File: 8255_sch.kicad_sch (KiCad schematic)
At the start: 3 parts, among them U2 8255, U5 8255, U6 8255

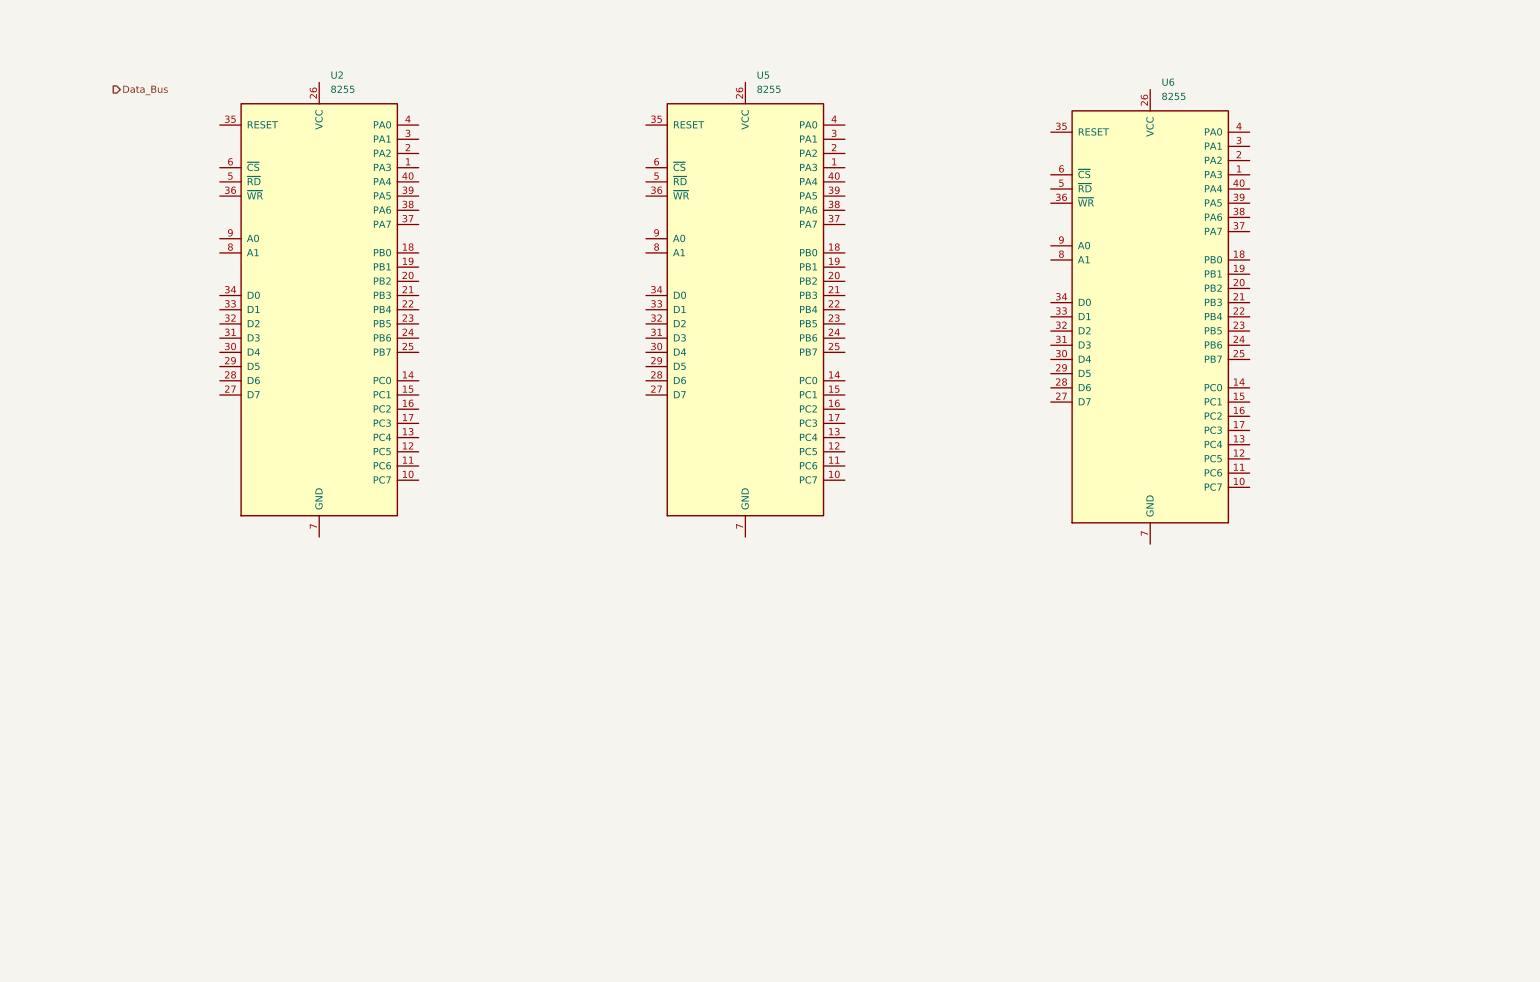
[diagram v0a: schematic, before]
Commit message: Wired up Decoding of 8255s, 8254, and 8279
Also fixed up the decoding for the 16550 and the 8259 as well as labeled all wires into/from the bus.
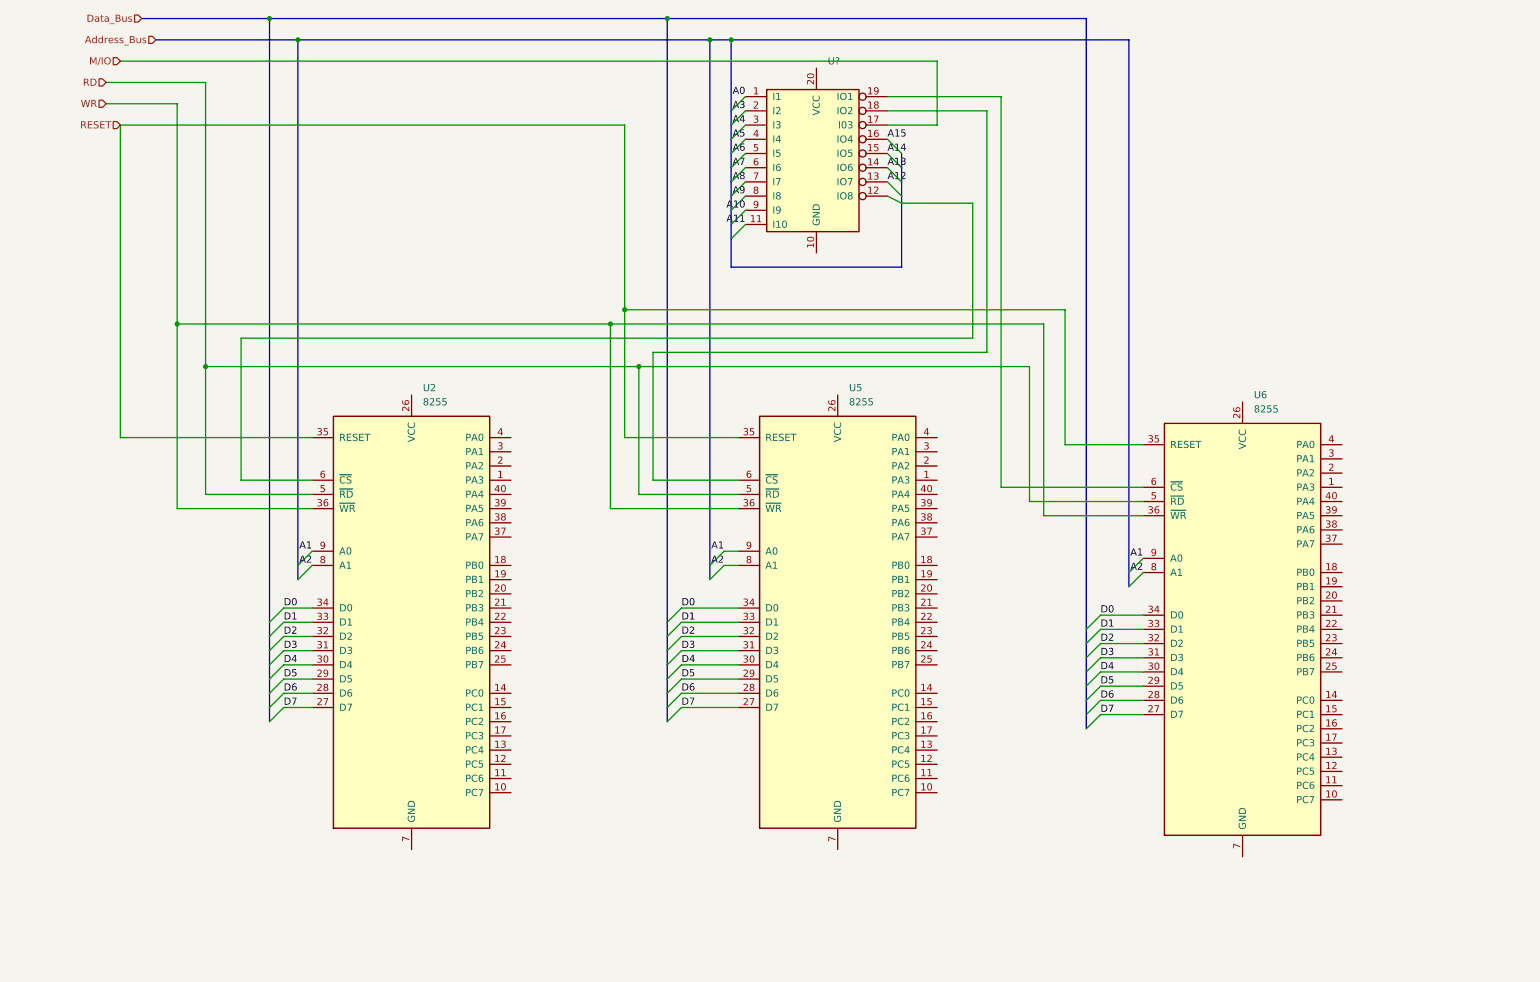
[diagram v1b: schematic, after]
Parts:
- added U?: (no value), symbol Logic_Programmable:PAL16L8
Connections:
- net D7: now reaches U2.27 (D7)
- net D7: now also U5.27 (D7), U6.27 (D7)
- net D6: now reaches U2.28 (D6)
- net D6: now also U5.28 (D6), U6.28 (D6)
- net D5: now reaches U2.29 (D5)
- net D5: now also U5.29 (D5), U6.29 (D5)
- net D4: now reaches U2.30 (D4)
- net D4: now also U5.30 (D4), U6.30 (D4)
- net D3: now reaches U2.31 (D3)
- net D3: now also U5.31 (D3), U6.31 (D3)
- net D2: now reaches U2.32 (D2)
- net D2: now also U5.32 (D2), U6.32 (D2)
- net D1: now reaches U2.33 (D1)
- net D1: now also U5.33 (D1), U6.33 (D1)
- net D0: now reaches U2.34 (D0)
- net D0: now also U5.34 (D0), U6.34 (D0)
- net RESET: now reaches U2.35 (RESET)
- net RESET: now also U5.35 (RESET), U6.35 (RESET)
- net WR: now reaches U2.36 (~{WR})
- net WR: now also U5.36 (~{WR}), U6.36 (~{WR})
- net RD: now reaches U2.5 (~{RD})
- net RD: now also U5.5 (~{RD}), U6.5 (~{RD})
- net at U2.6 (~{CS}): now also U?.12 (IO8)
- net A2: now reaches U2.8 (A1)
- net A2: now also U5.8 (A1), U6.8 (A1)
- net A1: now reaches U2.9 (A0)
- net A1: now also U5.9 (A0), U6.9 (A0)
- net at U6.6 (~{CS}): now also U?.19 (IO1)
- net at U5.6 (~{CS}): now also U?.18 (IO2)
- new net A0: U?.1 (I1)
- new net A10: U?.9 (I9)
- new net A11: U?.11 (I10)
- new net A12: U?.13 (IO7)
- new net A13: U?.14 (IO6)
- new net A14: U?.15 (IO5)
- new net A15: U?.16 (IO4)
- new net A3: U?.2 (I2)
- new net A4: U?.3 (I3)
- new net A5: U?.4 (I4)
- new net A6: U?.5 (I5)
- new net A7: U?.6 (I6)
- new net A8: U?.7 (I7)
- new net A9: U?.8 (I8)
- new net M/IO: U?.17 (I03)
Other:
- moved on the sheet: U2, U5, U6

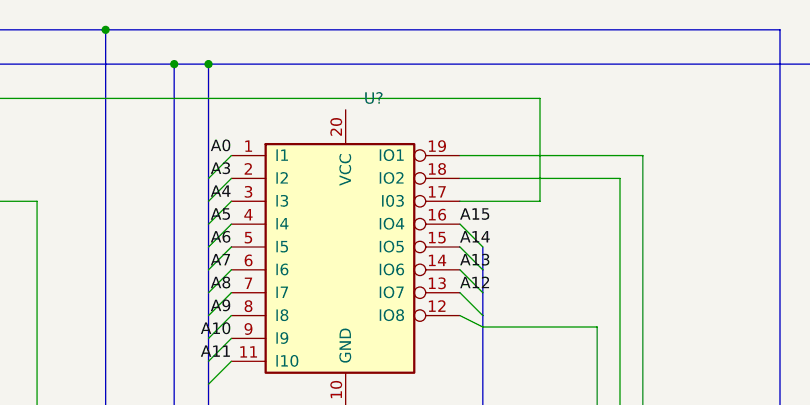
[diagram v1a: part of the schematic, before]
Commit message: Wired the max235 and DSUB9
We will double check the wiring tomorrow. Also added the data bus
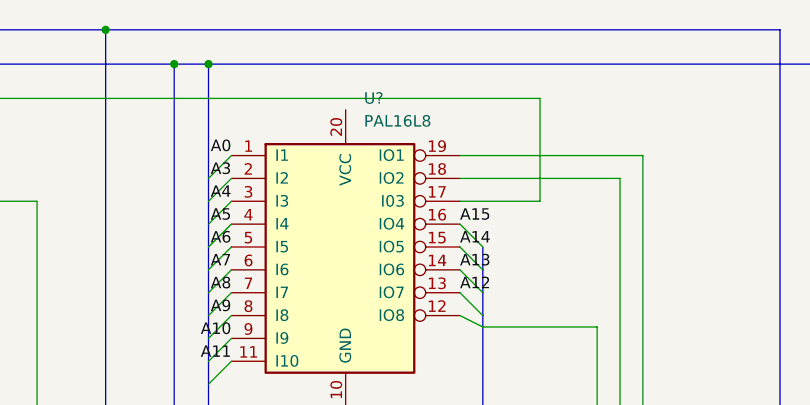
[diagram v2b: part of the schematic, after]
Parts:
- U?: value (none) -> PAL16L8
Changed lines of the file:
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@@
       (effects (font (size 1.27 1.27)) (justify left))
     )
-    (property "Value" "" (id 1) (at 149.3394 26.67 0)
+    (property "Value" "PAL16L8" (id 1) (at 149.3394 26.67 0)
       (effects (font (size 1.27 1.27)) (justify left))
     )

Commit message: Redid Bus
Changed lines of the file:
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@@
+    (stroke (width 0) (type default) (color 0 0 0 0))
+  )
+  (bus_entry (at 17.78 29.21) (size 2.54 2.54)
+    (stroke (width 0) (type default) (color 0 0 0 0))
+  )
+  (bus_entry (at 17.78 25.4) (size 2.54 2.54)
+    (stroke (width 0) (type default) (color 0 0 0 0))
+  )
+  (bus_entry (at 17.78 21.59) (size 2.54 2.54)
     (stroke (width 0) (type default) (color 0 0 0 0))
   )
@@
     (stroke (width 0) (type default) (color 0 0 0 0))
   )
-  (wire (pts (xy 22.86 24.13) (xy 168.91 24.13))
+  (wire (pts (xy 20.32 24.13) (xy 166.37 24.13))
     (stroke (width 0) (type default) (color 0 0 0 0))
   )
@@
     (stroke (width 0) (type default) (color 0 0 0 0))
   )
-  (wire (pts (xy 168.91 24.13) (xy 168.91 35.56))
+  (wire (pts (xy 166.37 24.13) (xy 168.91 35.56))
     (stroke (width 0) (type default) (color 0 0 0 0))
   )
@@
     (stroke (width 0) (type default) (color 0 0 0 0))
   )
-  (bus (pts (xy 29.21 20.32) (xy 54.61 20.32))
+  (bus (pts (xy 26.67 20.32) (xy 54.61 20.32))
     (stroke (width 0) (type default) (color 0 0 0 0))
   )
@@
     (stroke (width 0) (type default) (color 0 0 0 0))
   )
+  (bus (pts (xy 17.78 21.59) (xy 17.78 25.4))
+    (stroke (width 0) (type default) (color 0 0 0 0))
+  )
   (wire (pts (xy 175.26 73.66) (xy 175.26 49.53))
     (stroke (width 0) (type default) (color 0 0 0 0))
@@
     (stroke (width 0) (type default) (color 0 0 0 0))
   )
+  (bus (pts (xy 17.78 29.21) (xy 17.78 31.75))
+    (stroke (width 0) (type default) (color 0 0 0 0))
+  )
   (wire (pts (xy 187.96 71.12) (xy 187.96 105.41))
     (stroke (width 0) (type default) (color 0 0 0 0))
@@
     (stroke (width 0) (type default) (color 0 0 0 0))
   )
+  (bus (pts (xy 17.78 25.4) (xy 17.78 29.21))
+    (stroke (width 0) (type default) (color 0 0 0 0))
+  )
   (wire (pts (xy 113.03 68.58) (xy 191.77 68.58))
     (stroke (width 0) (type default) (color 0 0 0 0))
@@
     (effects (font (size 1.27 1.27)) (justify right bottom))
   )
+  (label "M{slash}IO" (at 20.32 24.13 0)
+    (effects (font (size 1.27 1.27)) (justify left bottom))
+  )
   (label "D4" (at 198.12 133.35 0)
     (effects (font (size 1.27 1.27)) (justify left bottom))
   )
+  (label "WR" (at 20.32 31.75 0)
+    (effects (font (size 1.27 1.27)) (justify left bottom))
+  )
   (label "A3" (at 134.62 33.02 180)
     (effects (font (size 1.27 1.27)) (justify right bottom))
@@
   (label "A2" (at 130.81 114.3 180)
     (effects (font (size 1.27 1.27)) (justify right bottom))
+  )
+  (label "RD" (at 20.32 27.94 0)
+    (effects (font (size 1.27 1.27)) (justify left bottom))
   )
   (label "A6" (at 134.62 40.64 180)
@@
     (effects (font (size 1.27 1.27)) (justify right))
   )
-  (hierarchical_label "M{slash}IO" (shape input) (at 22.86 24.13 180)
+  (hierarchical_label "ControlBus" (shape input) (at 17.78 21.59 180)
     (effects (font (size 1.27 1.27)) (justify right))
   )
-  (hierarchical_label "WR" (shape input) (at 20.32 31.75 180)
+  (hierarchical_label "Address_Bus" (shape input) (at 26.67 20.32 180)
     (effects (font (size 1.27 1.27)) (justify right))
   )
-  (hierarchical_label "Address_Bus" (shape input) (at 29.21 20.32 180)
-    (effects (font (size 1.27 1.27)) (justify right))
-  )
-  (hierarchical_label "RD" (shape input) (at 20.32 27.94 180)
-    (effects (font (size 1.27 1.27)) (justify right))
-  )

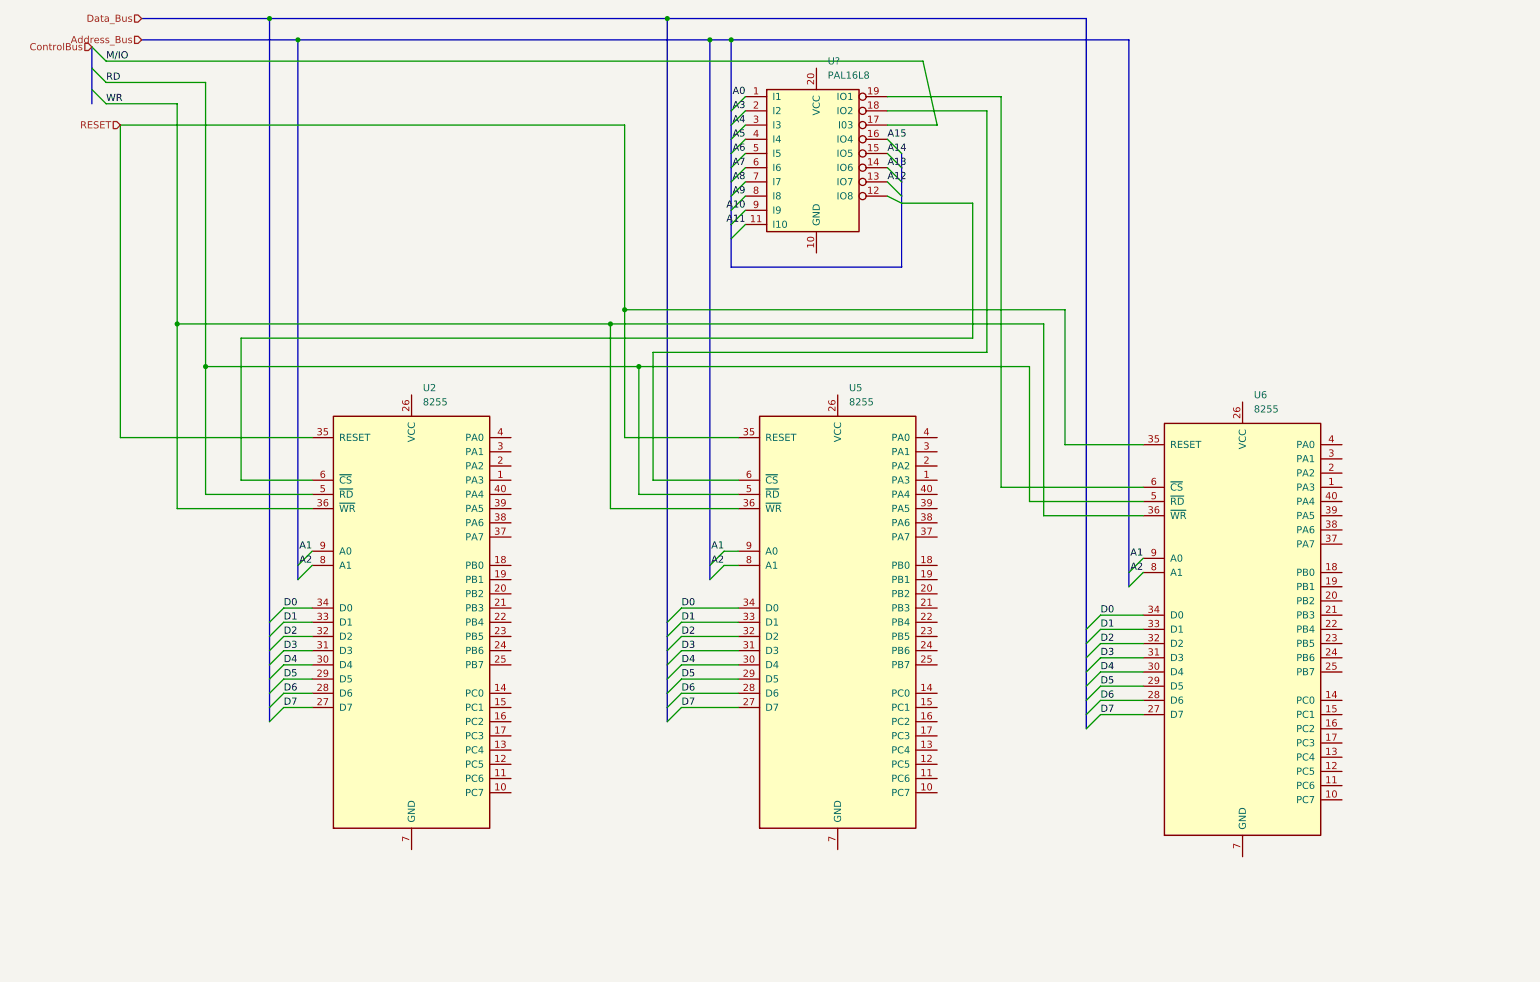
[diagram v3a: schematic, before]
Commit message: Added headers to the necessary pins, and created IO device sheet
Added headers for the three chips and for the busses. Also created and started to address  decode the actual IO components.
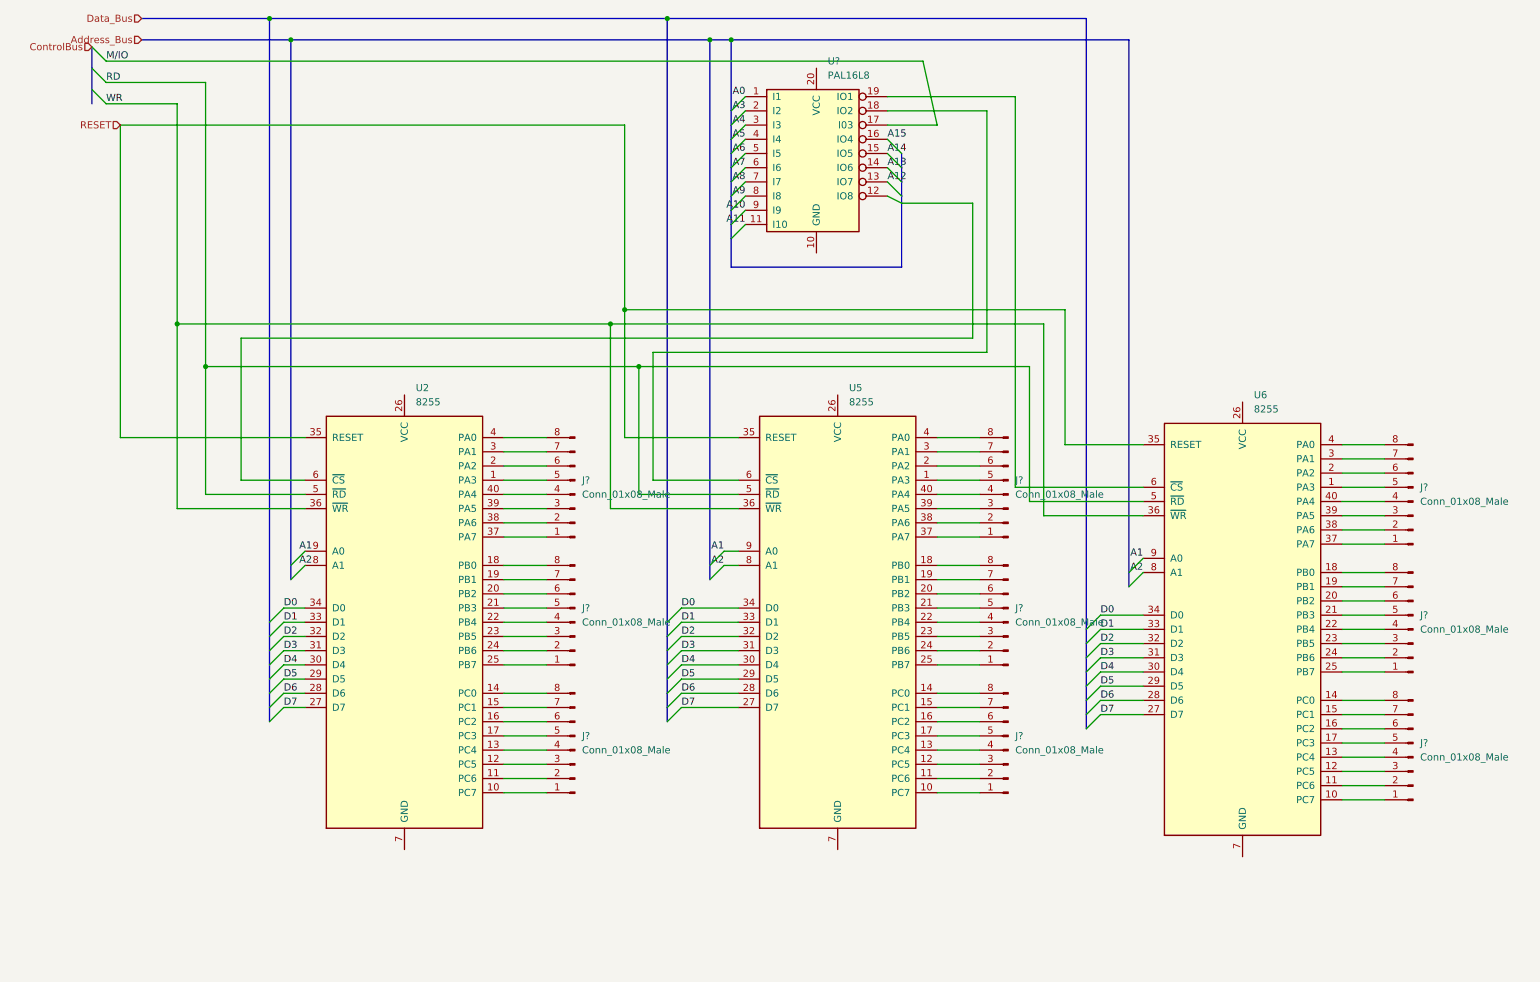
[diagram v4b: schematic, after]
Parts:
- added J? (x9): Conn_01x08_Male, symbol Connector:Conn_01x08_Male
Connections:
- net A1: no longer U2.9 (A0)
- net A2: no longer U2.8 (A1)
- net at U2.1 (PA3): now also J?.5 (Pin_5)
- net at U2.10 (PC7): now also J?.1 (Pin_1)
- net at U2.11 (PC6): now also J?.2 (Pin_2)
- net at U2.12 (PC5): now also J?.3 (Pin_3)
- net at U2.13 (PC4): now also J?.4 (Pin_4)
- net at U2.14 (PC0): now also J?.8 (Pin_8)
- net at U2.15 (PC1): now also J?.7 (Pin_7)
- net at U2.16 (PC2): now also J?.6 (Pin_6)
- net at U2.17 (PC3): now also J?.5 (Pin_5)
- net at U2.18 (PB0): now also J?.8 (Pin_8)
- net at U2.19 (PB1): now also J?.7 (Pin_7)
- net at U2.2 (PA2): now also J?.6 (Pin_6)
- net at U2.20 (PB2): now also J?.6 (Pin_6)
- net at U2.21 (PB3): now also J?.5 (Pin_5)
- net at U2.22 (PB4): now also J?.4 (Pin_4)
- net at U2.23 (PB5): now also J?.3 (Pin_3)
- net at U2.24 (PB6): now also J?.2 (Pin_2)
- net at U2.25 (PB7): now also J?.1 (Pin_1)
- net at U2.3 (PA1): now also J?.7 (Pin_7)
- net at U2.37 (PA7): now also J?.1 (Pin_1)
- net at U2.38 (PA6): now also J?.2 (Pin_2)
- net at U2.39 (PA5): now also J?.3 (Pin_3)
- net at U2.4 (PA0): now also J?.8 (Pin_8)
- net at U2.40 (PA4): now also J?.4 (Pin_4)
- net at U6.1 (PA3): now also J?.5 (Pin_5)
- net at U6.10 (PC7): now also J?.1 (Pin_1)
- net at U6.11 (PC6): now also J?.2 (Pin_2)
- net at U6.12 (PC5): now also J?.3 (Pin_3)
- net at U6.13 (PC4): now also J?.4 (Pin_4)
- net at U6.14 (PC0): now also J?.8 (Pin_8)
- net at U6.15 (PC1): now also J?.7 (Pin_7)
- net at U6.16 (PC2): now also J?.6 (Pin_6)
- net at U6.17 (PC3): now also J?.5 (Pin_5)
- net at U6.18 (PB0): now also J?.8 (Pin_8)
- net at U6.19 (PB1): now also J?.7 (Pin_7)
- net at U6.2 (PA2): now also J?.6 (Pin_6)
- net at U6.20 (PB2): now also J?.6 (Pin_6)
- net at U6.21 (PB3): now also J?.5 (Pin_5)
- net at U6.22 (PB4): now also J?.4 (Pin_4)
- net at U6.23 (PB5): now also J?.3 (Pin_3)
- net at U6.24 (PB6): now also J?.2 (Pin_2)
- net at U6.25 (PB7): now also J?.1 (Pin_1)
- net at U6.3 (PA1): now also J?.7 (Pin_7)
- net at U6.37 (PA7): now also J?.1 (Pin_1)
- net at U6.38 (PA6): now also J?.2 (Pin_2)
- net at U6.39 (PA5): now also J?.3 (Pin_3)
- net at U6.4 (PA0): now also J?.8 (Pin_8)
- net at U6.40 (PA4): now also J?.4 (Pin_4)
- net at U5.1 (PA3): now also J?.5 (Pin_5)
- net at U5.10 (PC7): now also J?.1 (Pin_1)
- net at U5.11 (PC6): now also J?.2 (Pin_2)
- net at U5.12 (PC5): now also J?.3 (Pin_3)
- net at U5.13 (PC4): now also J?.4 (Pin_4)
- net at U5.14 (PC0): now also J?.8 (Pin_8)
- net at U5.15 (PC1): now also J?.7 (Pin_7)
- net at U5.16 (PC2): now also J?.6 (Pin_6)
- net at U5.17 (PC3): now also J?.5 (Pin_5)
- net at U5.18 (PB0): now also J?.8 (Pin_8)
- net at U5.19 (PB1): now also J?.7 (Pin_7)
- net at U5.2 (PA2): now also J?.6 (Pin_6)
- net at U5.20 (PB2): now also J?.6 (Pin_6)
- net at U5.21 (PB3): now also J?.5 (Pin_5)
- net at U5.22 (PB4): now also J?.4 (Pin_4)
- net at U5.23 (PB5): now also J?.3 (Pin_3)
- net at U5.24 (PB6): now also J?.2 (Pin_2)
- net at U5.25 (PB7): now also J?.1 (Pin_1)
- net at U5.3 (PA1): now also J?.7 (Pin_7)
- net at U5.37 (PA7): now also J?.1 (Pin_1)
- net at U5.38 (PA6): now also J?.2 (Pin_2)
- net at U5.39 (PA5): now also J?.3 (Pin_3)
- net at U5.4 (PA0): now also J?.8 (Pin_8)
- net at U5.40 (PA4): now also J?.4 (Pin_4)
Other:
- moved on the sheet: U2
